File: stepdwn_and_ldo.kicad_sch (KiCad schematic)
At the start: 1 part

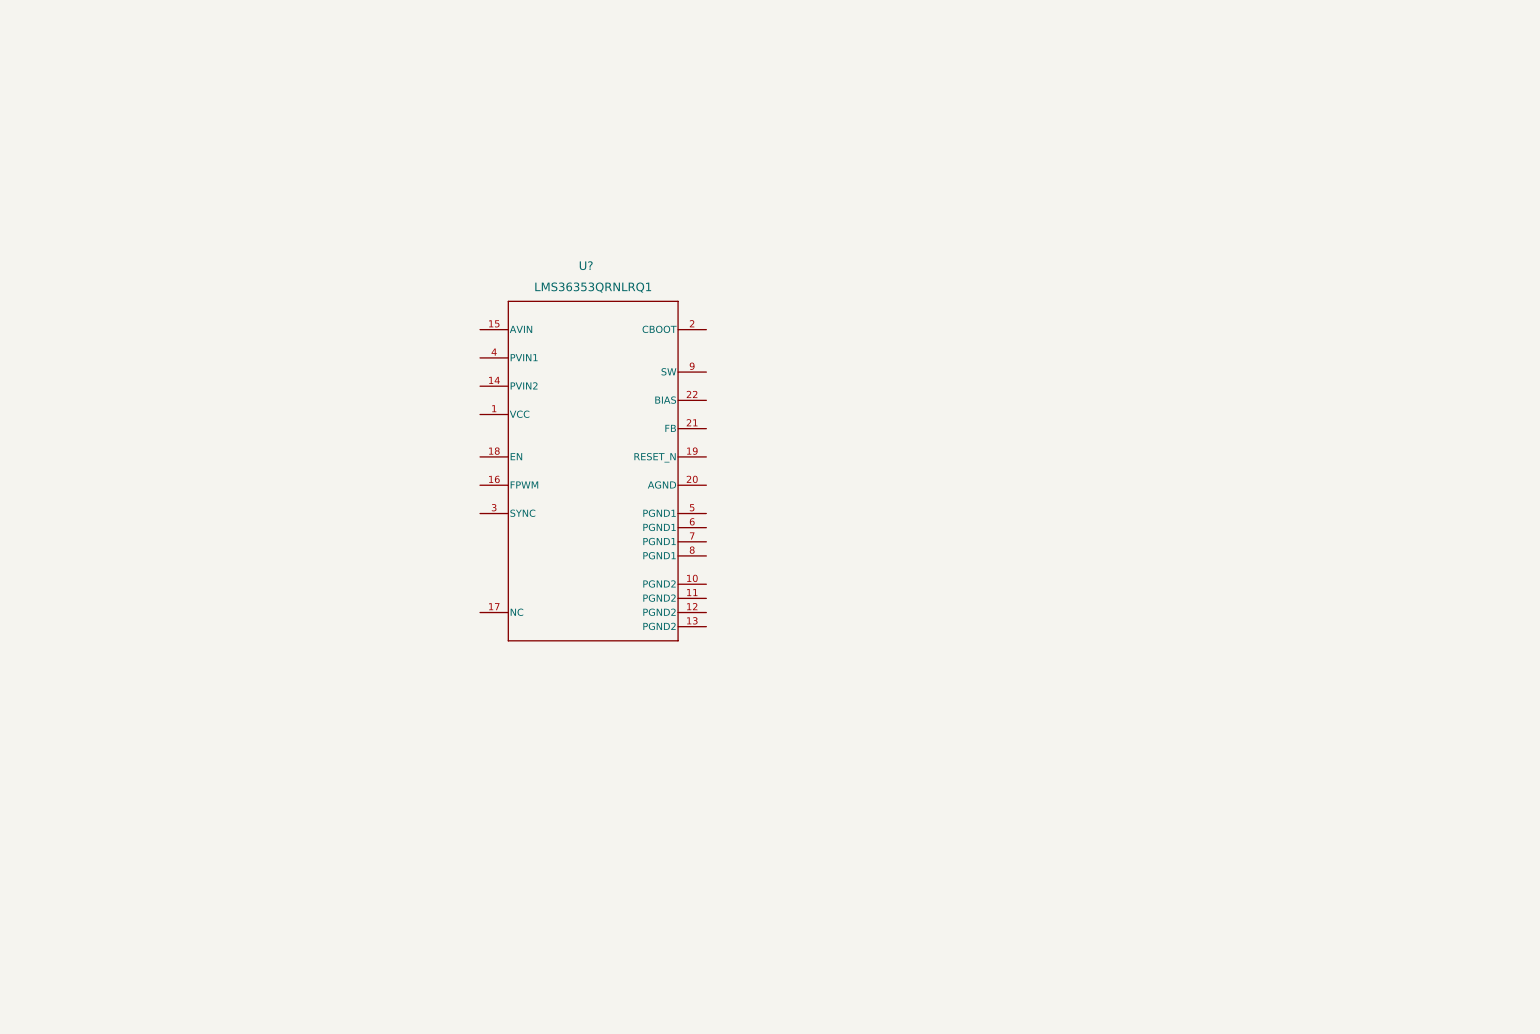
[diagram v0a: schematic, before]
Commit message: finished BQ charge controller
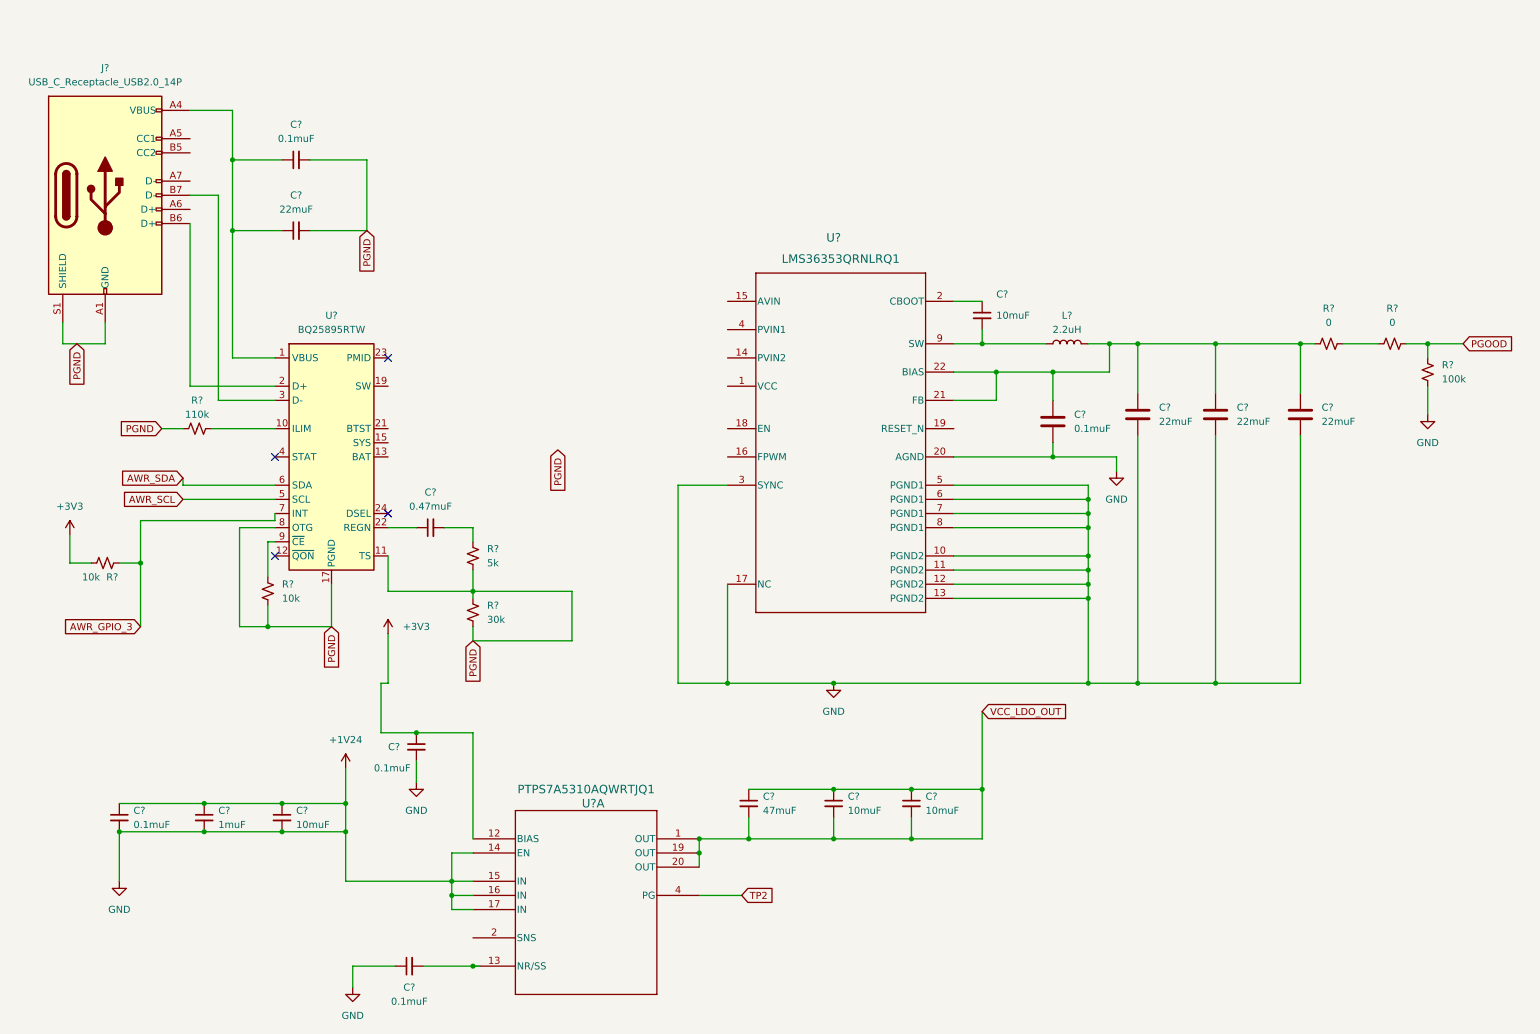
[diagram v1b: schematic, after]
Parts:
- added C? (x3): 22muF, symbol Device:C
- added C? (x4): 0.1muF, symbol Device:C_Small
- added C? (x4): 10muF, symbol Device:C_Small
- added C?: 0.47muF, symbol Device:C_Small
- added C?: 0.1muF, symbol Device:C
- added C?: 47muF, symbol Device:C_Small
- added C?: 22muF, symbol Device:C_Small
- added C?: 1muF, symbol Device:C_Small
- added J?: USB_C_Receptacle_USB2.0_14P, symbol Connector:USB_C_Receptacle_USB2.0_14P
- added L?: 2.2uH, symbol Device:L
- added R? (x2): 0, symbol Device:R_Small_US
- added R?: 110k, symbol Device:R_Small_US
- added R?: 100k, symbol Device:R_Small_US
- added R?: 5k, symbol Device:R_Small_US
- added R? (x2): 10k, symbol Device:R_Small_US
- added R?: 30k, symbol Device:R_Small_US
- added U?: PTPS7A5310AQWRTJQ1, WQFN20_RTJ_TEX, symbol TPS7A5301QRGRRQ1:PTPS7A5310AQWRTJQ1
- added U?: BQ25895RTW, Package_DFN_QFN:Texas_RTW_WQFN-24-1EP_4x4mm_P0.5mm_EP2.7x2.7mm_ThermalVias, symbol Battery_Management:BQ25895RTW
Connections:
- net +1V35: now reaches U?.10 (PGND2)
- net +1V35: now also U?.11 (PGND2), U?.12 (PGND2), U?.13 (PGND2), U?.17 (NC), U?.20 (AGND), U?.3 (SYNC), U?.5 (PGND1), U?.6 (PGND1), U?.7 (PGND1), U?.8 (PGND1), C?.1, C?.1, C?.1, C?.1, C?.2, C?.2, C?.2, C?.2, C?.2, C?.2, C?.2, C?.2, R?.1, U?.14 (EN), U?.15 (IN), U?.16 (IN), U?.17 (IN)
- net at U?.2 (CBOOT): now also C?.1
- net at U?.21 (FB): now also U?.22 (BIAS), C?.1, C?.1, C?.1, C?.1, L?.2, R?.1
- net at U?.9 (SW): now also C?.2, L?.1
- new net: C?.2, U?.13 (NR/SS)
- new net: R?.1, R?.2
- new net: R?.2, U?.10 (ILIM)
- new net: C?.1, U?.22 (REGN)
- new net: C?.2, R?.2
- new net: C?.1, C?.1, J?.A4 (VBUS), J?.A9 (VBUS), J?.B4 (VBUS), J?.B9 (VBUS), U?.1 (VBUS)
- new net: U?.13 (BAT), U?.14 (BAT)
- new net: U?.15 (SYS), U?.16 (SYS)
- new net: U?.19 (SW), U?.20 (SW)
- new net: J?.B6 (D+), U?.2 (D+)
- new net: J?.B7 (D-), U?.3 (D-)
- new net: R?.2, U?.9 (~{CE})
- new net +3V3: C?.1, R?.1, U?.12 (BIAS)
- new net AWR_GPIO_3: R?.2, U?.7 (INT)
- new net AWR_SCL: U?.5 (SCL)
- new net AWR_SDA: U?.6 (SDA)
- new net PGND: C?.2, C?.2, J?.A1 (GND), J?.A12 (GND), J?.B1 (GND), J?.B12 (GND), J?.S1 (SHIELD), R?.1, R?.1, R?.1, R?.1, R?.2, U?.11 (TS), U?.17 (PGND), U?.18 (PGND), U?.25 (PGND), U?.8 (OTG)
- new net PGOOD: R?.2, R?.2
- new net TP2: U?.4 (PG)
- new net VCC_LDO_OUT: C?.1, C?.1, C?.1, C?.2, C?.2, C?.2, U?.1 (OUT), U?.19 (OUT), U?.20 (OUT)
- no-connect marks 0 -> 4
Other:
- moved on the sheet: U?

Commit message: finishing power sschematics
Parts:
- added C?: 47muF, symbol Device:C_Small
- added C? (x3): 10muf, symbol Device:C_Small
- added C? (x2): 22muF/50V, symbol Device:C_Small
- added C? (x2): 4.7muF, symbol Device:C_Small
- added C? (x2): 10muF, symbol Device:C_Small
- added C?: 0.47muF, symbol Device:C_Small
- added F?: 5A, symbol Device:Fuse
- added L?: L, symbol Device:L
- added L?: 2.2uH, symbol Device:L
- added R?: 10k, symbol Device:R_Small_US
- added TH?: 10k, symbol Device:Thermistor_NTC
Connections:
- net +1V35: now also U?.14 (PVIN2), U?.15 (AVIN), U?.16 (FPWM), U?.4 (PVIN1), C?.1, C?.1, C?.1, C?.2, C?.2, C?.2, C?.2, C?.2, C?.2, C?.2, L?.1, R?.1
- net PGND: now also C?.1, C?.1, C?.2, TH?.2; no longer R?.1, R?.2, U?.11 (TS)
- net at U?.1 (VCC): now also C?.1
- net at U?.18 (EN): now also R?.2
- net at U?.13 (BAT), U?.14 (BAT): now also C?.1
- net at U?.15 (SYS), U?.16 (SYS): now also C?.2, C?.2, L?.2
- net at U?.19 (SW), U?.20 (SW): now also C?.2, L?.1
- net at U?.21 (BTST): now also C?.1
- new net: C?.1, C?.1, C?.1, F?.1, L?.2
- new net: R?.1, R?.2, TH?.1, U?.11 (TS)
- new net SYS: F?.2
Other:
- moved on the sheet: C?, L?, R?, U?

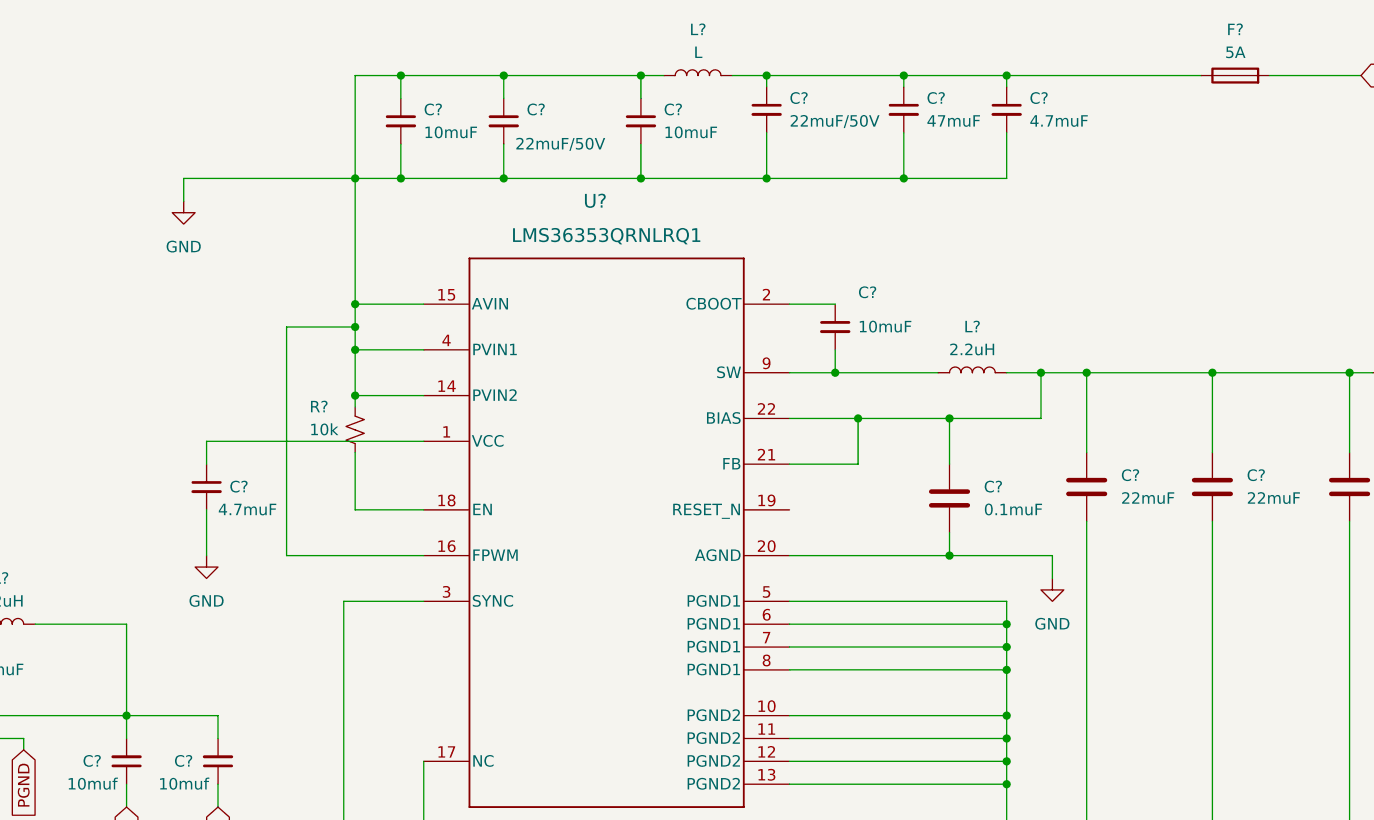
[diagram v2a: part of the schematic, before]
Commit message: squasing ERC errors
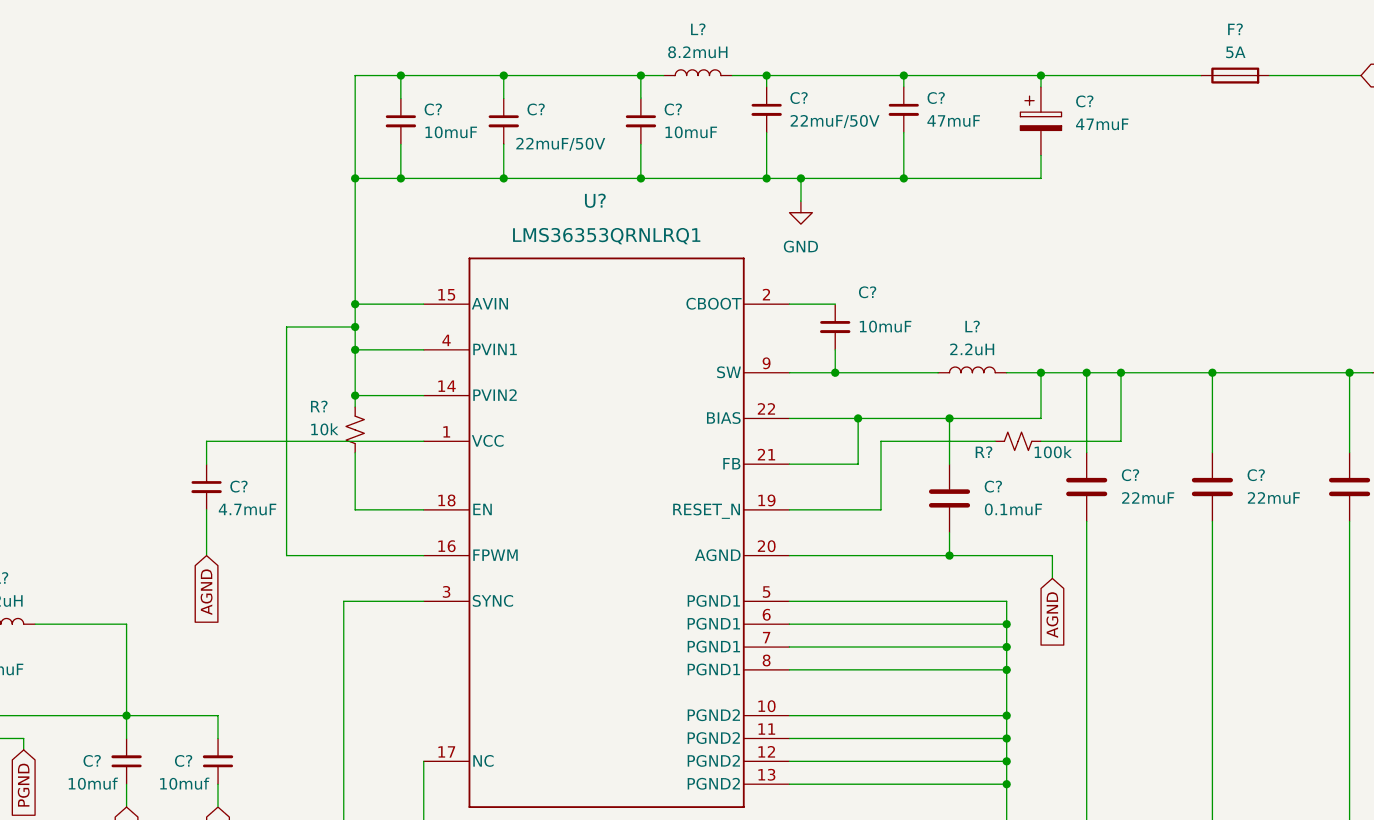
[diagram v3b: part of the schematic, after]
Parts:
- removed C?: 4.7muF, symbol Device:C_Small
- added C?: 47muF, symbol Device:C_Polarized
- added R?: 100k, symbol Device:R_Small_US
- L?: value L -> 8.2muH
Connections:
- net +1V35: now also C?.2; no longer C?.2, C?.2, U?.20 (AGND)
- net at C?.1, C?.1, C?.1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: now also R?.1
- net at U?.19 (RESET_N): now also R?.2
- net at C?.1, C?.1, F?.1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: now also C?.1
- new net AGND: C?.2, C?.2, U?.20 (AGND)

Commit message: squased errors going over supply desgin
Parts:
- added R10, R11: 5k, symbol Device:R_Small_US
- gave numbers to parts that had none: 46
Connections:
- net +1V35 is gone; now on net GND: C32.1, C32.2, C33.1, C33.2, C34.1, C34.2, C37.1, C38.2, C45.1, C45.2, C47.1, C47.2, C49.1, C49.2, C51.2, C53.2, C55.2, C56.2, C57.2, C58.2, L5.1, R21.1, R25.1, U4.14 (EN), U4.15 (IN), U4.16 (IN), U4.17 (IN), U5.10 (PGND2), U5.11 (PGND2), U5.12 (PGND2), U5.13 (PGND2), U5.14 (PVIN2), U5.15 (AVIN), U5.16 (FPWM), U5.17 (NC), U5.3 (SYNC), U5.4 (PVIN1), U5.5 (PGND1), U5.6 (PGND1), U5.7 (PGND1), U5.8 (PGND1)
- net VCC_LDO_OUT is gone; now on net GND: C46.1, C46.2, C48.1, C48.2, C50.1, C50.2, U4.1 (OUT), U4.19 (OUT), U4.20 (OUT)
- net +3V3: now also C54.1, C56.1, C57.1, C58.1, L6.2, R22.1, R23.1, U5.21 (FB), U5.22 (BIAS)
- net PGND: now also R10.1, R11.2
- net GND: now reaches U4.2 (SNS)
- net at J1.A5 (CC1): now also R11.1
- net at J1.B5 (CC2): now also R10.2
- no-connect marks 4 -> 6
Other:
- moved on the sheet: C46

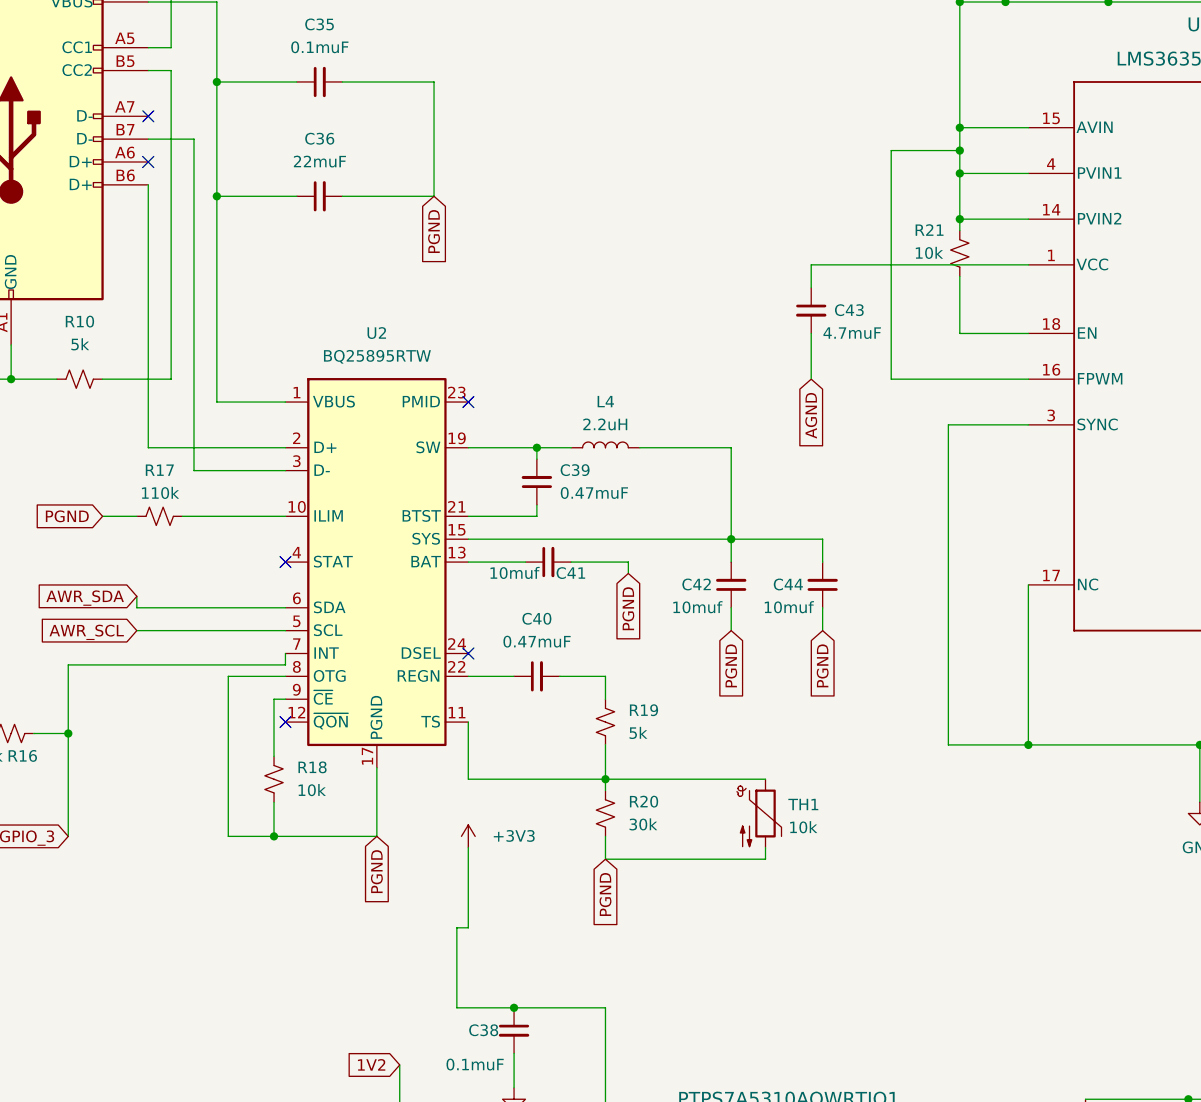
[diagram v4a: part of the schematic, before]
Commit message: enabling OTG pin and PMID for 5v output
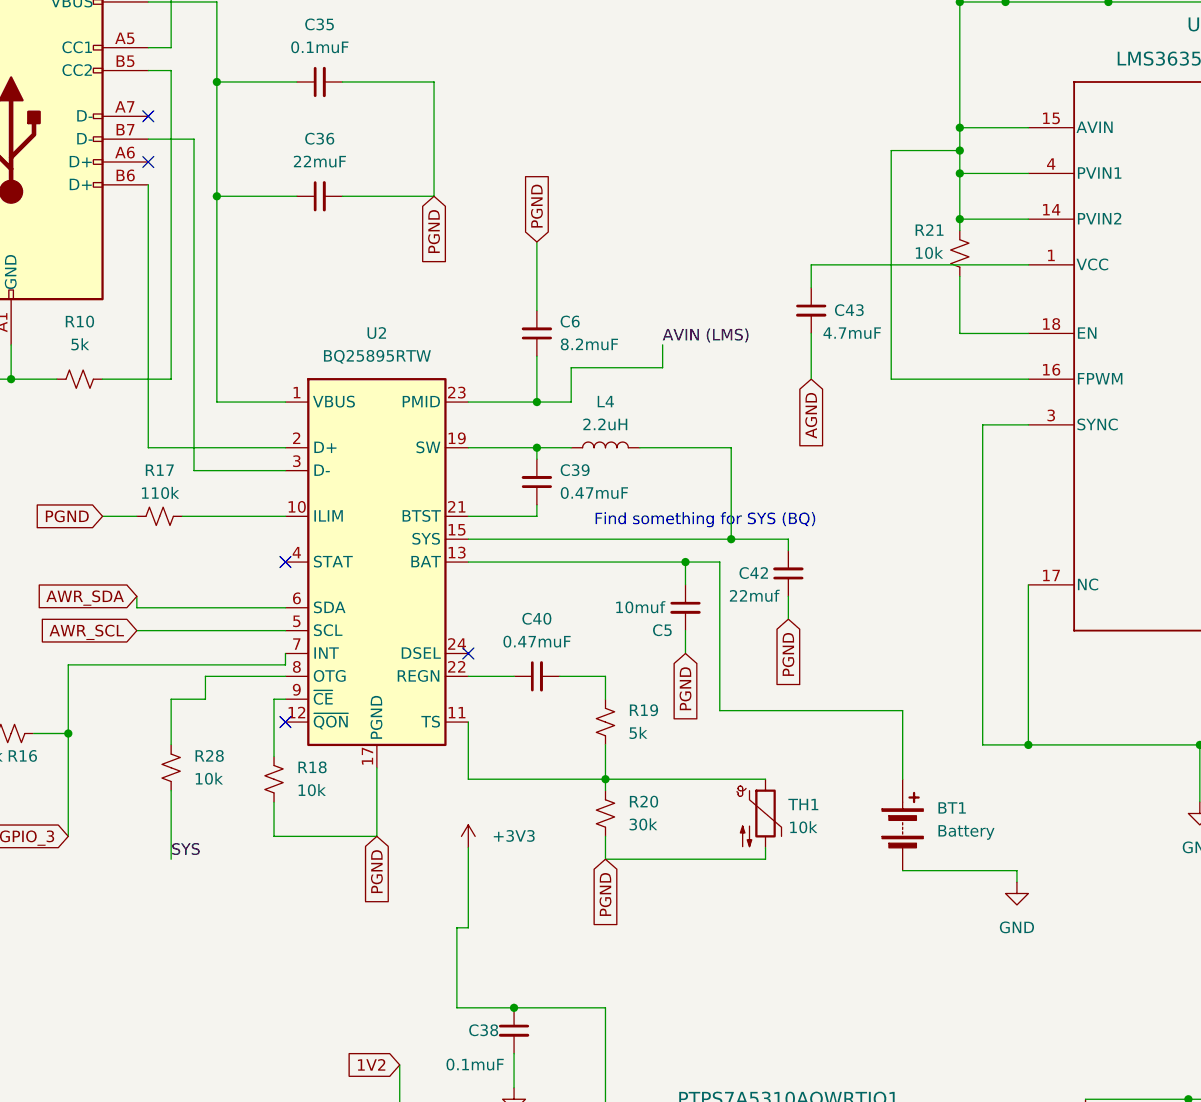
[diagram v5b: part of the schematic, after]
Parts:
- removed C41, C44: 10muf, symbol Device:C_Small
- added BT1: Battery, symbol Device:Battery
- added C5: 10muf, symbol Device:C_Small
- added C6: 8.2muF, symbol Device:C_Small
- added R28: 10k, symbol Device:R_Small_US
- C42: value 10muf -> 22muf
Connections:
- net GND: now also BT1.2 (-)
- net PGND: now also C5.2, C6.2; no longer U2.8 (OTG)
- net SYS: now also R28.1
- net at U2.13 (BAT), U2.14 (BAT): now also BT1.1 (+), C5.1
- net AVIN (LMS): now reaches U2.23 (PMID)
- net AVIN (LMS): now also C6.1
- new net: R28.2, U2.8 (OTG)
- no-connect marks 6 -> 5
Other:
- note added: "Find something for SYS (BQ)"
- moved on the sheet: C42
